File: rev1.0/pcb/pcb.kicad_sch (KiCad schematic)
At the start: 15 parts, among them J1 AVR-ISP-6, SW1 SW_Push, U1 ATMEGA32U4, Y1 16MHz

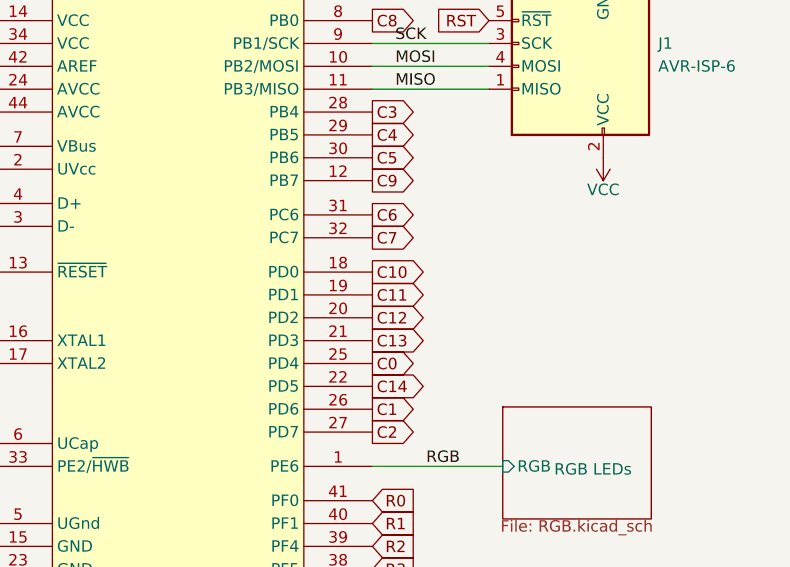
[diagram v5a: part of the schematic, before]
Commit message: colums, rows and RGB done
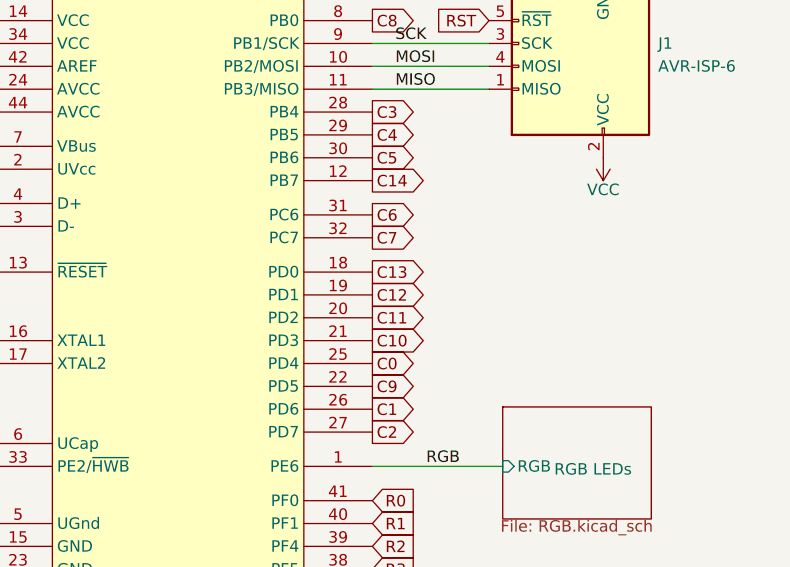
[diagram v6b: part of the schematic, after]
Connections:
- net C10: now also U1.21 (PD3); no longer U1.18 (PD0)
- net C11: now also U1.20 (PD2); no longer U1.19 (PD1)
- net C12: now also U1.19 (PD1); no longer U1.20 (PD2)
- net C13: now also U1.18 (PD0); no longer U1.21 (PD3)
- net C14: now also U1.12 (PB7); no longer U1.22 (PD5)
- net C9: now also U1.22 (PD5); no longer U1.12 (PB7)
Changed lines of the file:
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@@
     (comment 1 "Conor Burns")
   )
+  (junction (at 59.436 28.067) (diameter 0) (color 0 0 0 0))
+  (junction (at 87.63 35.687) (diameter 0) (color 0 0 0 0))
+  (junction (at 70.612 67.945) (diameter 0) (color 0 0 0 0))
+  (junction (at 65.024 33.147) (diameter 0) (color 0 0 0 0))
+  (junction (at 76.454 33.147) (diameter 0) (color 0 0 0 0))
+  (junction (at 76.454 28.067) (diameter 0) (color 0 0 0 0))
   (junction (at 89.408 83.947) (diameter 0) (color 0 0 0 0))
-  (junction (at 59.436 28.067) (diameter 0) (color 0 0 0 0))
+  (junction (at 89.408 95.377) (diameter 0) (color 0 0 0 0))
+  (junction (at 87.63 28.067) (diameter 0) (color 0 0 0 0))
+  (junction (at 70.612 33.147) (diameter 0) (color 0 0 0 0))
+  (junction (at 70.612 63.627) (diameter 0) (color 0 0 0 0))
+  (junction (at 89.408 85.217) (diameter 0) (color 0 0 0 0))
+  (junction (at 65.024 28.067) (diameter 0) (color 0 0 0 0))
+  (junction (at 70.612 28.067) (diameter 0) (color 0 0 0 0))
+  (junction (at 89.408 92.837) (diameter 0) (color 0 0 0 0))
+  (junction (at 85.598 83.947) (diameter 0) (color 0 0 0 0))
+  (junction (at 89.408 42.037) (diameter 0) (color 0 0 0 0))
+  (junction (at 89.408 87.757) (diameter 0) (color 0 0 0 0))
+  (junction (at 82.296 28.067) (diameter 0) (color 0 0 0 0))
+  (junction (at 81.534 59.309) (diameter 0) (color 0 0 0 0))
+  (junction (at 89.408 35.687) (diameter 0) (color 0 0 0 0))
+  (junction (at 59.436 33.147) (diameter 0) (color 0 0 0 0))
+  (junction (at 81.534 67.945) (diameter 0) (color 0 0 0 0))
+  (junction (at 89.408 90.297) (diameter 0) (color 0 0 0 0))
   (junction (at 89.408 28.067) (diameter 0) (color 0 0 0 0))
-  (junction (at 89.408 35.687) (diameter 0) (color 0 0 0 0))
-  (junction (at 89.408 87.757) (diameter 0) (color 0 0 0 0))
-  (junction (at 70.612 67.945) (diameter 0) (color 0 0 0 0))
-  (junction (at 70.612 33.147) (diameter 0) (color 0 0 0 0))
-  (junction (at 65.024 28.067) (diameter 0) (color 0 0 0 0))
-  (junction (at 89.408 42.037) (diameter 0) (color 0 0 0 0))
-  (junction (at 81.534 67.945) (diameter 0) (color 0 0 0 0))
-  (junction (at 76.454 33.147) (diameter 0) (color 0 0 0 0))
-  (junction (at 65.024 33.147) (diameter 0) (color 0 0 0 0))
-  (junction (at 87.63 35.687) (diameter 0) (color 0 0 0 0))
-  (junction (at 70.612 28.067) (diameter 0) (color 0 0 0 0))
-  (junction (at 89.408 95.377) (diameter 0) (color 0 0 0 0))
-  (junction (at 89.408 90.297) (diameter 0) (color 0 0 0 0))
-  (junction (at 82.296 28.067) (diameter 0) (color 0 0 0 0))
-  (junction (at 70.612 63.627) (diameter 0) (color 0 0 0 0))
-  (junction (at 85.598 83.947) (diameter 0) (color 0 0 0 0))
   (junction (at 62.23 62.611) (diameter 0) (color 0 0 0 0))
-  (junction (at 89.408 85.217) (diameter 0) (color 0 0 0 0))
-  (junction (at 87.63 28.067) (diameter 0) (color 0 0 0 0))
-  (junction (at 81.534 59.309) (diameter 0) (color 0 0 0 0))
-  (junction (at 89.408 92.837) (diameter 0) (color 0 0 0 0))
-  (junction (at 59.436 33.147) (diameter 0) (color 0 0 0 0))
-  (junction (at 76.454 28.067) (diameter 0) (color 0 0 0 0))
   (no_connect (at 89.408 31.877))
   (wire (pts (xy 89.408 83.947) (xy 85.598 83.947))
@@
     (stroke (width 0) (type solid) (color 0 0 0 0))
   )
+  (wire (pts (xy 81.534 83.947) (xy 85.598 83.947))
+    (stroke (width 0) (type solid) (color 0 0 0 0))
+  )
   (wire (pts (xy 81.534 82.931) (xy 81.534 83.947))
     (stroke (width 0) (type solid) (color 0 0 0 0))
   )
-  (wire (pts (xy 81.534 83.947) (xy 85.598 83.947))
-    (stroke (width 0) (type solid) (color 0 0 0 0))
-  )
   (wire (pts (xy 81.534 73.787) (xy 89.408 73.787))
     (stroke (width 0) (type solid) (color 0 0 0 0))
@@
     (stroke (width 0) (type solid) (color 0 0 0 0))
   )
+  (wire (pts (xy 76.454 33.147) (xy 82.296 33.147))
+    (stroke (width 0) (type solid) (color 0 0 0 0))
+  )
+  (wire (pts (xy 70.612 33.147) (xy 76.454 33.147))
+    (stroke (width 0) (type solid) (color 0 0 0 0))
+  )
+  (wire (pts (xy 65.024 33.147) (xy 70.612 33.147))
+    (stroke (width 0) (type solid) (color 0 0 0 0))
+  )
   (wire (pts (xy 59.436 33.147) (xy 65.024 33.147))
     (stroke (width 0) (type solid) (color 0 0 0 0))
   )
-  (wire (pts (xy 70.612 33.147) (xy 76.454 33.147))
-    (stroke (width 0) (type solid) (color 0 0 0 0))
-  )
-  (wire (pts (xy 65.024 33.147) (xy 70.612 33.147))
-    (stroke (width 0) (type solid) (color 0 0 0 0))
-  )
-  (wire (pts (xy 76.454 33.147) (xy 82.296 33.147))
-    (stroke (width 0) (type solid) (color 0 0 0 0))
-  )
   (wire (pts (xy 81.534 67.945) (xy 89.408 67.945))
     (stroke (width 0) (type solid) (color 0 0 0 0))
@@
     (stroke (width 0) (type solid) (color 0 0 0 0))
   )
+  (wire (pts (xy 89.408 42.037) (xy 89.408 43.307))
+    (stroke (width 0) (type solid) (color 0 0 0 0))
+  )
   (wire (pts (xy 89.408 40.767) (xy 89.408 42.037))
     (stroke (width 0) (type solid) (color 0 0 0 0))
   )
-  (wire (pts (xy 89.408 42.037) (xy 89.408 43.307))
-    (stroke (width 0) (type solid) (color 0 0 0 0))
-  )
   (wire (pts (xy 132.588 34.417) (xy 145.542 34.417))
     (stroke (width 0) (type solid) (color 0 0 0 0))
@@
     (stroke (width 0) (type solid) (color 0 0 0 0))
   )
+  (wire (pts (xy 89.408 83.947) (xy 89.408 85.217))
+    (stroke (width 0) (type solid) (color 0 0 0 0))
+  )
+  (wire (pts (xy 89.408 85.217) (xy 89.408 87.757))
+    (stroke (width 0) (type solid) (color 0 0 0 0))
+  )
   (wire (pts (xy 89.408 82.677) (xy 89.408 83.947))
     (stroke (width 0) (type solid) (color 0 0 0 0))
   )
-  (wire (pts (xy 89.408 83.947) (xy 89.408 85.217))
-    (stroke (width 0) (type solid) (color 0 0 0 0))
-  )
-  (wire (pts (xy 89.408 85.217) (xy 89.408 87.757))
-    (stroke (width 0) (type solid) (color 0 0 0 0))
-  )
   (wire (pts (xy 89.408 87.757) (xy 89.408 90.297))
     (stroke (width 0) (type solid) (color 0 0 0 0))
@@
     (stroke (width 0) (type solid) (color 0 0 0 0))
   )
+  (wire (pts (xy 76.454 28.067) (xy 82.296 28.067))
+    (stroke (width 0) (type solid) (color 0 0 0 0))
+  )
   (wire (pts (xy 70.612 28.067) (xy 76.454 28.067))
     (stroke (width 0) (type solid) (color 0 0 0 0))
   )
   (wire (pts (xy 65.024 28.067) (xy 70.612 28.067))
-    (stroke (width 0) (type solid) (color 0 0 0 0))
-  )
-  (wire (pts (xy 76.454 28.067) (xy 82.296 28.067))
     (stroke (width 0) (type solid) (color 0 0 0 0))
   )
@@
     )
   )
-  (global_label "C11" (shape output) (at 132.588 57.277 0) (fields_autoplaced)
-    (effects (font (size 1.27 1.27)) (justify left))
-    (property "Intersheet References" "${INTERSHEET_REFS}" (id 0) (at 138.5948 57.1976 0)
+  (global_label "C11" (shape output) (at 132.588 59.817 0) (fields_autoplaced)
+    (effects (font (size 1.27 1.27)) (justify left))
+    (property "Intersheet References" "${INTERSHEET_REFS}" (id 0) (at 138.5948 59.7376 0)
       (effects (font (size 1.27 1.27)) (justify left) hide)
     )
@@
     )
   )
-  (global_label "C13" (shape output) (at 132.588 62.357 0) (fields_autoplaced)
-    (effects (font (size 1.27 1.27)) (justify left))
-    (property "Intersheet References" "${INTERSHEET_REFS}" (id 0) (at 138.5948 62.2776 0)
-      (effects (font (size 1.27 1.27)) (justify left) hide)
-    )
-  )
-  (global_label "C14" (shape output) (at 132.588 67.437 0) (fields_autoplaced)
-    (effects (font (size 1.27 1.27)) (justify left))
-    (property "Intersheet References" "${INTERSHEET_REFS}" (id 0) (at 138.6901 67.3576 0)
+  (global_label "C13" (shape output) (at 132.588 54.737 0) (fields_autoplaced)
+    (effects (font (size 1.27 1.27)) (justify left))
+    (property "Intersheet References" "${INTERSHEET_REFS}" (id 0) (at 138.5948 54.6576 0)
+      (effects (font (size 1.27 1.27)) (justify left) hide)
+    )
+  )
+  (global_label "C14" (shape output) (at 132.588 44.577 0) (fields_autoplaced)
+    (effects (font (size 1.27 1.27)) (justify left))
+    (property "Intersheet References" "${INTERSHEET_REFS}" (id 0) (at 138.6901 44.4976 0)
       (effects (font (size 1.27 1.27)) (justify left) hide)
     )
@@
     )
   )
-  (global_label "C12" (shape output) (at 132.588 59.817 0) (fields_autoplaced)
-    (effects (font (size 1.27 1.27)) (justify left))
-    (property "Intersheet References" "${INTERSHEET_REFS}" (id 0) (at 138.5948 59.7376 0)
+  (global_label "C12" (shape output) (at 132.588 57.277 0) (fields_autoplaced)
+    (effects (font (size 1.27 1.27)) (justify left))
+    (property "Intersheet References" "${INTERSHEET_REFS}" (id 0) (at 138.5948 57.1976 0)
       (effects (font (size 1.27 1.27)) (justify left) hide)
     )
@@
     )
   )
-  (global_label "C9" (shape output) (at 132.588 44.577 0) (fields_autoplaced)
-    (effects (font (size 1.27 1.27)) (justify left))
-    (property "Intersheet References" "${INTERSHEET_REFS}" (id 0) (at 137.3853 44.4976 0)
+  (global_label "C9" (shape output) (at 132.588 67.437 0) (fields_autoplaced)
+    (effects (font (size 1.27 1.27)) (justify left))
+    (property "Intersheet References" "${INTERSHEET_REFS}" (id 0) (at 137.3853 67.3576 0)
       (effects (font (size 1.27 1.27)) (justify left) hide)
     )
@@
     )
   )
-  (global_label "C10" (shape output) (at 132.588 54.737 0) (fields_autoplaced)
-    (effects (font (size 1.27 1.27)) (justify left))
-    (property "Intersheet References" "${INTERSHEET_REFS}" (id 0) (at 138.5948 54.6576 0)
+  (global_label "C10" (shape output) (at 132.588 62.357 0) (fields_autoplaced)
+    (effects (font (size 1.27 1.27)) (justify left))
+    (property "Intersheet References" "${INTERSHEET_REFS}" (id 0) (at 138.5948 62.2776 0)
       (effects (font (size 1.27 1.27)) (justify left) hide)
     )
@@
     )
     (path "/b0becbd9-ae71-4e25-bcb7-574f7aadd0b6/2b6c5633-7e5f-435a-9743-fb679aa56463"
-      (reference "#PWR?") (unit 1) (value "GND") (footprint "")
+      (reference "#PWR0101") (unit 1) (value "GND") (footprint "")
     )
     (path "/b595cb0d-4c23-49e2-8fcb-9629550bac58"
